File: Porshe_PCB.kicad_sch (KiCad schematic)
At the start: 37 parts, among them IC1 RASPBERRY_PI_PICO_W, J1 Conn_01x04_Socket, J10 Conn_01x03_Socket, J11 Conn_01x04_Socket, J12 Conn_01x01_Pin, J13 Conn_01x20_Socket, J2 SM04B-SRSS-TB_LF__SN_, J3 Conn_01x04_Socket, J4 S2B-PH-SM4-TB_LF__SN_, J5 Screw_Terminal_01x03, J6 Conn_01x01_Pin, J7 Conn_01x01_Pin, J8 Conn_01x01_Pin, J9 Conn_01x20_Socket, Q1 DMG2305UX-7, U1 DS3231SN, U2 AHT20

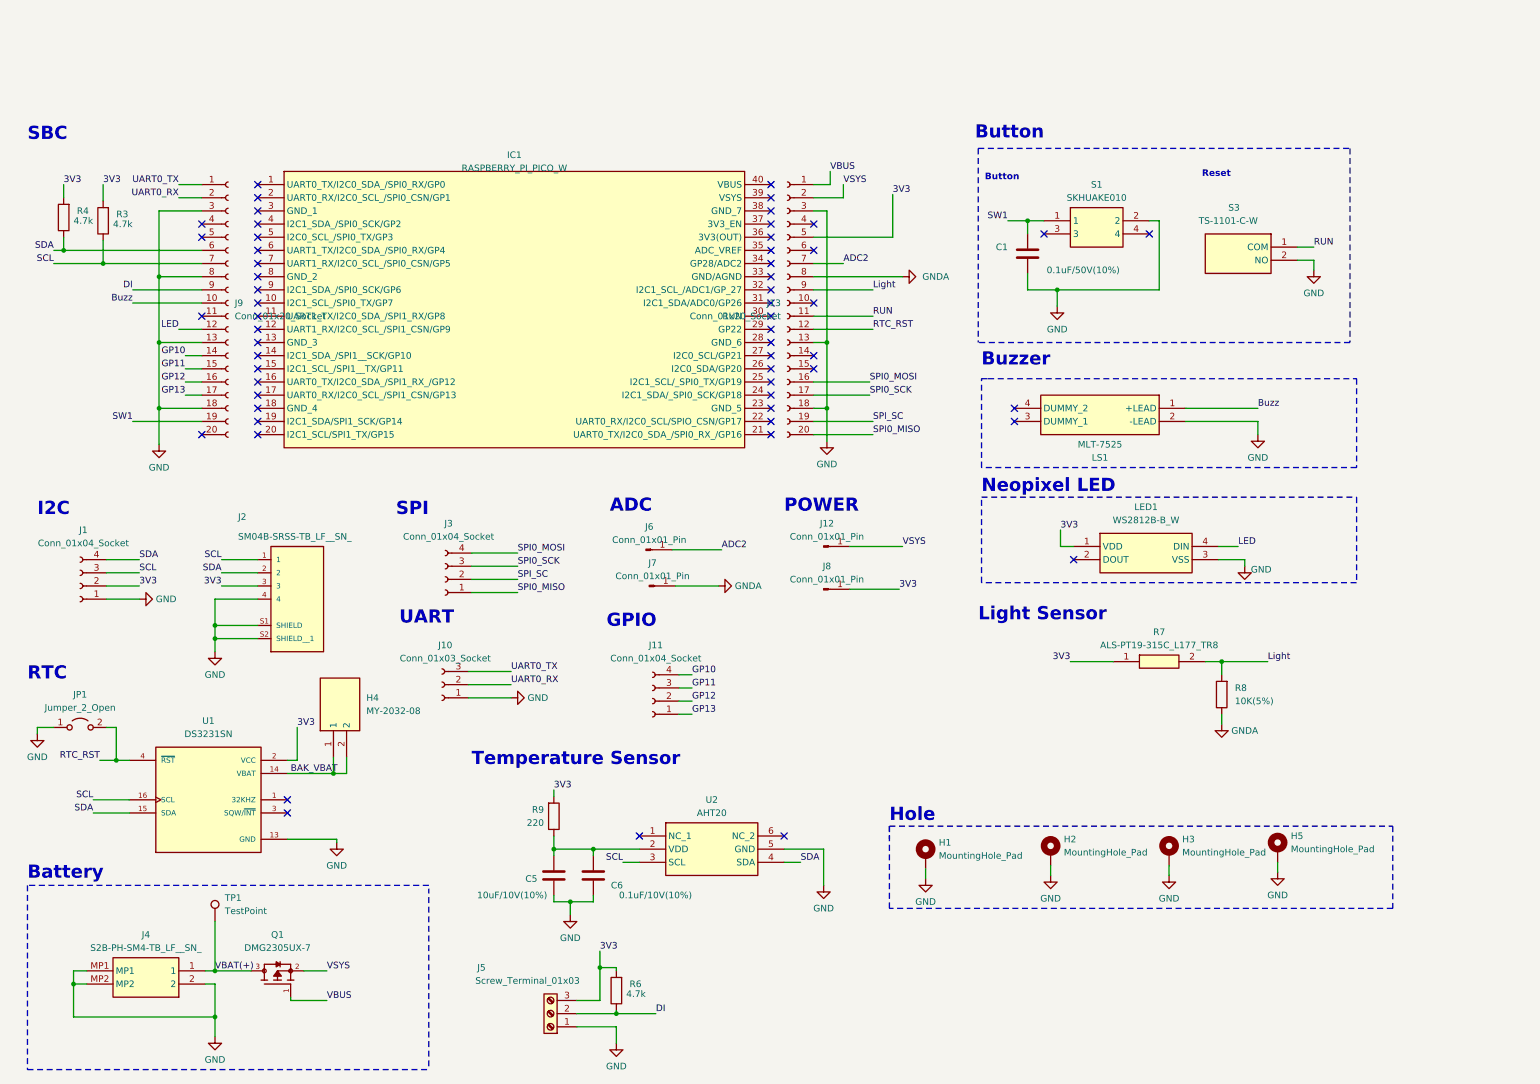
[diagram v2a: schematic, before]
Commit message: BOM확인후 부품 배치완료
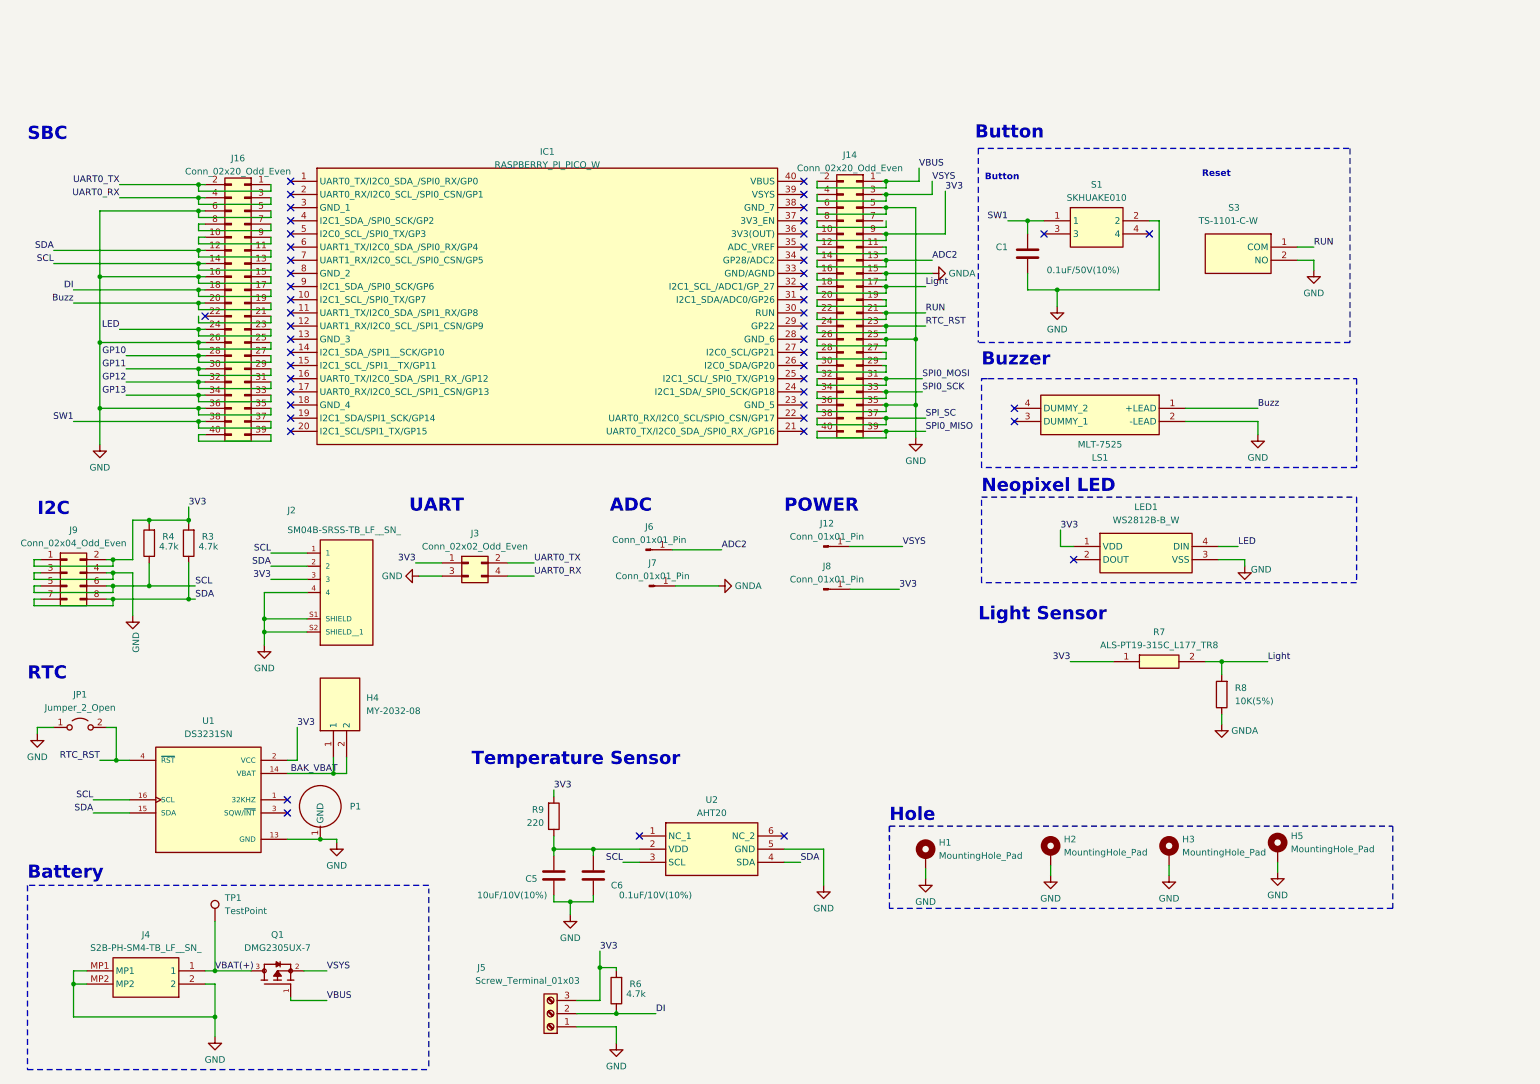
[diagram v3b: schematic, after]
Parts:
- removed J1, J11: Conn_01x04_Socket, symbol Connector:Conn_01x04_Socket
- removed J10: Conn_01x03_Socket, Connector_PinSocket_2.54mm:PinSocket_1x03_P2.54mm_Vertical_SMD_Pin1Left, symbol Connector:Conn_01x03_Socket
- removed J13: Conn_01x20_Socket, Connector_PinSocket_2.54mm:PinSocket_1x20_P2.54mm_Vertical_SMD_Pin1Right, symbol Connector:Conn_01x20_Socket
- removed J3: Conn_01x04_Socket, Connector_PinSocket_2.54mm:PinSocket_1x04_P2.54mm_Vertical, symbol Connector:Conn_01x04_Socket
- removed J9: Conn_01x20_Socket, Connector_PinSocket_2.54mm:PinSocket_1x20_P2.54mm_Vertical_SMD_Pin1Left, symbol Connector:Conn_01x20_Socket
- added J14, J16: Conn_02x20_Odd_Even, Connector_PinSocket_2.54mm:PinSocket_2x20_P2.54mm_Vertical_SMD, symbol Connector_Generic:Conn_02x20_Odd_Even
- added J3: Conn_02x02_Odd_Even, Connector_PinSocket_2.54mm:PinSocket_2x02_P2.54mm_Vertical_SMD, symbol Connector_Generic:Conn_02x02_Odd_Even
- added J9: Conn_02x04_Odd_Even, Connector_PinSocket_2.54mm:PinSocket_2x04_P2.54mm_Vertical_SMD, symbol Connector_Generic:Conn_02x04_Odd_Even
- added P1: ~, ConCell_GND:CR2032_GND, symbol CoinCell_GND:CR2032_GND
- C1: footprint Capacitor_Tantalum_SMD:CP_EIA-1608-08_AVX-J_Pad1.25x1.05mm_HandSolder -> Capacitor_SMD:C_0603_1608Metric; LCSC Part # (none) -> C14663
- C5: footprint Capacitor_Tantalum_SMD:CP_EIA-1608-10_AVX-L_Pad1.25x1.05mm_HandSolder -> Capacitor_SMD:C_0603_1608Metric; LCSC Part # (none) -> C19702
- C6: footprint Capacitor_Tantalum_SMD:CP_EIA-1608-10_AVX-L_Pad1.25x1.05mm_HandSolder -> Capacitor_SMD:C_0603_1608Metric; LCSC Part # (none) -> C519438
- H1, H2, H3, H5, J12, J6, J7, J8, JP1, TP1: now left out of the parts list
- H4: JLCPCB Part # (none) -> C964831
- J2: LCSC Part # (none) -> C160404
- J4: LCSC Part # (none) -> C295747
- J5: LCSC Part # (none) -> C695630
- LED1: JLCPCB Part # (none) -> C2761795
- Q1: LCSC Part # (none) -> C150470
- R7: LCSC Part # (none) -> C146233
- U2: LCSC Part # (none) -> C2757850
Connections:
- net 3V3: now also J14.10 (Pin_10), J14.9 (Pin_9), J3.1 (Pin_1), J9.1 (Pin_1), J9.2 (Pin_2)
- net ADC2: now also J14.13 (Pin_13), J14.14 (Pin_14)
- net Buzz: now also J16.19 (Pin_19), J16.20 (Pin_20)
- net DI: now also J16.17 (Pin_17), J16.18 (Pin_18)
- net GND: now also J14.25 (Pin_25), J14.26 (Pin_26), J14.35 (Pin_35), J14.36 (Pin_36), J14.5 (Pin_5), J14.6 (Pin_6), J16.15 (Pin_15), J16.16 (Pin_16), J16.25 (Pin_25), J16.26 (Pin_26), J16.35 (Pin_35), J16.36 (Pin_36), J16.5 (Pin_5), J16.6 (Pin_6), J3.3 (Pin_3), J9.3 (Pin_3), J9.4 (Pin_4), P1.1 (GND)
- net GNDA: now also J14.15 (Pin_15), J14.16 (Pin_16)
- net GP10: now also J16.27 (Pin_27), J16.28 (Pin_28)
- net GP11: now also J16.29 (Pin_29), J16.30 (Pin_30)
- net GP12: now also J16.31 (Pin_31), J16.32 (Pin_32)
- net GP13: now also J16.33 (Pin_33), J16.34 (Pin_34)
- net LED: now also J16.23 (Pin_23), J16.24 (Pin_24)
- net Light: now also J14.17 (Pin_17), J14.18 (Pin_18)
- net RTC_RST: now also J14.23 (Pin_23), J14.24 (Pin_24)
- net RUN: now also J14.21 (Pin_21), J14.22 (Pin_22)
- net SCL: now also R4.1, J16.13 (Pin_13), J16.14 (Pin_14), J9.5 (Pin_5), J9.6 (Pin_6); no longer R3.1
- net SDA: now also R3.1, J16.11 (Pin_11), J16.12 (Pin_12), J9.7 (Pin_7), J9.8 (Pin_8); no longer R4.1
- net SPI0_MISO: now also J14.39 (Pin_39), J14.40 (Pin_40)
- net SPI0_MOSI: now also J14.31 (Pin_31), J14.32 (Pin_32)
- net SPI0_SCK: now also J14.33 (Pin_33), J14.34 (Pin_34)
- net SPI_SC: now also J14.37 (Pin_37), J14.38 (Pin_38)
- net SW1: now also J16.37 (Pin_37), J16.38 (Pin_38)
- net UART0_RX: now also J16.3 (Pin_3), J16.4 (Pin_4), J3.4 (Pin_4)
- net UART0_TX: now also J16.1 (Pin_1), J16.2 (Pin_2), J3.2 (Pin_2)
- net VBUS: now also J14.1 (Pin_1), J14.2 (Pin_2)
- net VSYS: now also J14.3 (Pin_3), J14.4 (Pin_4)
- new net: J16.10 (Pin_10), J16.9 (Pin_9)
- new net: J16.39 (Pin_39), J16.40 (Pin_40)
- new net: J16.7 (Pin_7), J16.8 (Pin_8)
- new net: J14.11 (Pin_11), J14.12 (Pin_12)
- new net: J14.19 (Pin_19), J14.20 (Pin_20)
- new net: J14.27 (Pin_27), J14.28 (Pin_28)
- new net: J14.29 (Pin_29), J14.30 (Pin_30)
- no-connect marks 58 -> 50
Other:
- note removed: "GPIO"
- note removed: "SPI"
- moved on the sheet: IC1, J2, R3, R4

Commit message: 회로도 완성
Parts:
- removed C5: 10uF/10V(10%), Capacitor_SMD:C_0603_1608Metric, symbol Device:C
- removed C6: 0.1uF/10V(10%), Capacitor_SMD:C_0603_1608Metric, symbol Device:C
- removed H5: MountingHole_Pad, MountingHole:MountingHole_2.7mm_M2.5_ISO7380_Pad_TopOnly, symbol Mechanical:MountingHole_Pad
- removed J5: Screw_Terminal_01x03, TerminalBlock_4Ucon:TerminalBlock_4Ucon_1x03_P3.50mm_Horizontal, symbol Connector:Screw_Terminal_01x03
- removed R7: ALS-PT19-315C_L177_TR8, ALSPT19315CL177TR8, symbol ALS-PT19-315C_L177_TR8:ALS-PT19-315C_L177_TR8
- removed U2: AHT20, AHT20, symbol AHT20:AHT20
- added C2: 1uF/50V(10%), Capacitor_SMD:C_0603_1608Metric, symbol Device:C
- added IC2: BH1750FVI-TR, WSOF6, symbol BH1750FVI-TR:BH1750FVI-TR
- added J1: TF-115, TF115, symbol TF-115:TF-115
- added J10, J11, J5: Conn_01x01_Pin, TestPoint:TestPoint_THTPad_D2.0mm_Drill1.0mm, symbol Connector:Conn_01x01_Pin
- added JP2: Jumper_2_Open, Jumper:SolderJumper-2_P1.3mm_Open_RoundedPad1.0x1.5mm, symbol Jumper:Jumper_2_Open
- added JP3: Jumper_2_Bridged, Jumper:SolderJumper-2_P1.3mm_Bridged_RoundedPad1.0x1.5mm, symbol Jumper:Jumper_2_Bridged
- added R1, R2: 4.7k, Resistor_SMD:R_0603_1608Metric_Pad0.98x0.95mm_HandSolder, symbol Device:R
- added R5: 1k, Resistor_SMD:R_0603_1608Metric_Pad0.98x0.95mm_HandSolder, symbol Device:R
- added R7: 10k, Resistor_SMD:R_0603_1608Metric_Pad0.98x0.95mm_HandSolder, symbol Device:R
- added TP2, TP3: TestPoint, TestPoint:TestPoint_Pad_D1.0mm, symbol Connector:TestPoint
- R8: value 10K(5%) -> 10k/1%
- R9: value 220 -> 10k/1%
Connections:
- net GP11 is gone; now on net SPI0_MOSI: J16.29 (Pin_29), J16.30 (Pin_30)
- net GP13 is gone; now on net LED: J16.33 (Pin_33), J16.34 (Pin_34)
- net 3V3: now also IC2.1 (VCC), J1.4 (VDD), J5.1 (Pin_1), JP2.1 (A), R1.2, R2.2, R5.2; no longer R9.2
- net DI: now also J10.1 (Pin_1)
- net GND: now also C2.1, IC2.3 (GND), J1.6 (VSS), J1.MP1, J1.MP2, J1.MP3, J1.MP4, J11.1 (Pin_1), R7.1
- net GNDA: no longer R8.1
- net LED: no longer J16.23 (Pin_23), J16.24 (Pin_24)
- net SCL: now also IC2.6 (SCL)
- net SDA: now also IC2.4 (SDA)
- net SPI0_MISO: now also J16.21 (Pin_21), J16.22 (Pin_22), J1.7 (DAT0); no longer J14.39 (Pin_39), J14.40 (Pin_40)
- net SPI0_MOSI: now also J1.3 (CMD); no longer J14.31 (Pin_31), J14.32 (Pin_32)
- net SPI0_SCK: now also J1.5 (CLX); no longer J14.33 (Pin_33), J14.34 (Pin_34)
- net SPI_SC: now also J16.23 (Pin_23), J16.24 (Pin_24), J1.1 (DAT2), R2.1; no longer J14.37 (Pin_37), J14.38 (Pin_38)
- net VBAT(+): now also R8.2, R9.2
- net at R9.1: now also R8.1, JP3.1 (A)
- net at J14.7 (Pin_7): now also J14.8 (Pin_8)
- net GP10 renamed SPI1_SCK
- net GP12 renamed Light_RST
- net Light_RST: now also IC2.5 (DVI)
- net Light renamed BAT_DIV
- net BAT_DIV: now also JP3.2 (B); no longer R8.2
- new net: J1.2 (CD/DAT3), R1.1
- new net: J1.8 (DAT1), TP2.1
- new net: J1.CD1, TP3.1
- new net: C2.2, R5.1
- new net: IC2.2 (ADDR), JP2.2 (B), R7.2
- new net: J14.31 (Pin_31), J14.32 (Pin_32)
- new net: J14.33 (Pin_33), J14.34 (Pin_34)
- new net: J14.37 (Pin_37), J14.38 (Pin_38)
- new net: J14.39 (Pin_39), J14.40 (Pin_40)
- no-connect marks 50 -> 47
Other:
- note added: "SDcard"
- note removed: "Temperature Sensor"
- moved on the sheet: R6

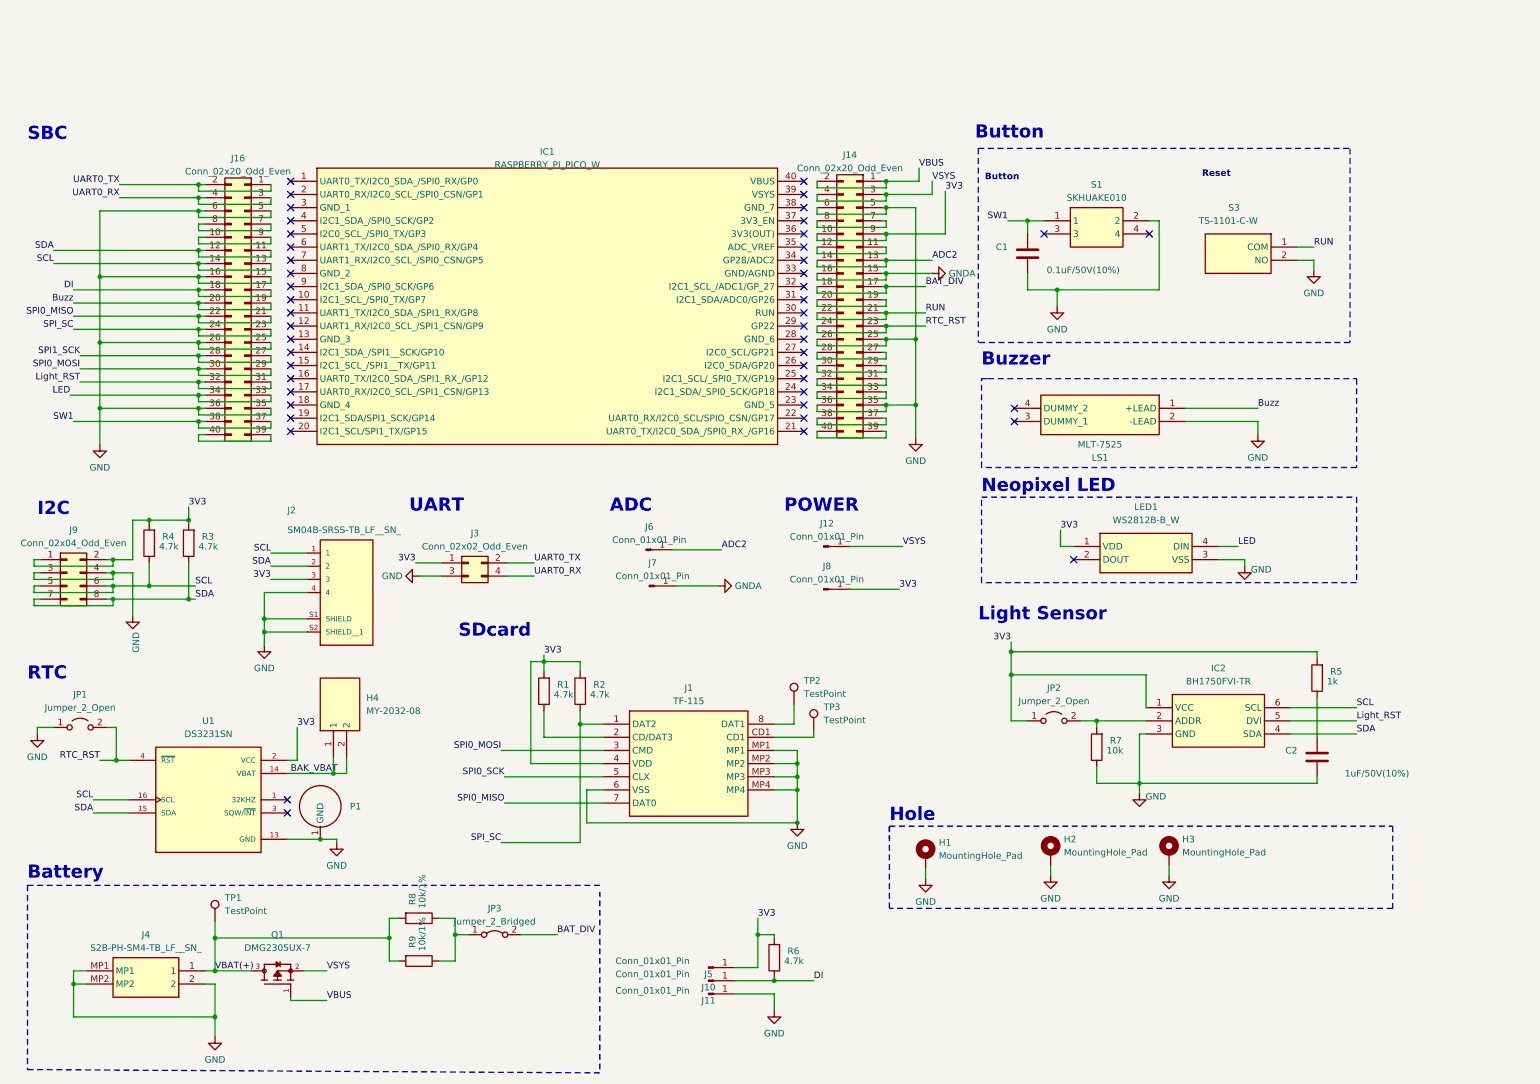
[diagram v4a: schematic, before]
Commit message: add smartfarm function
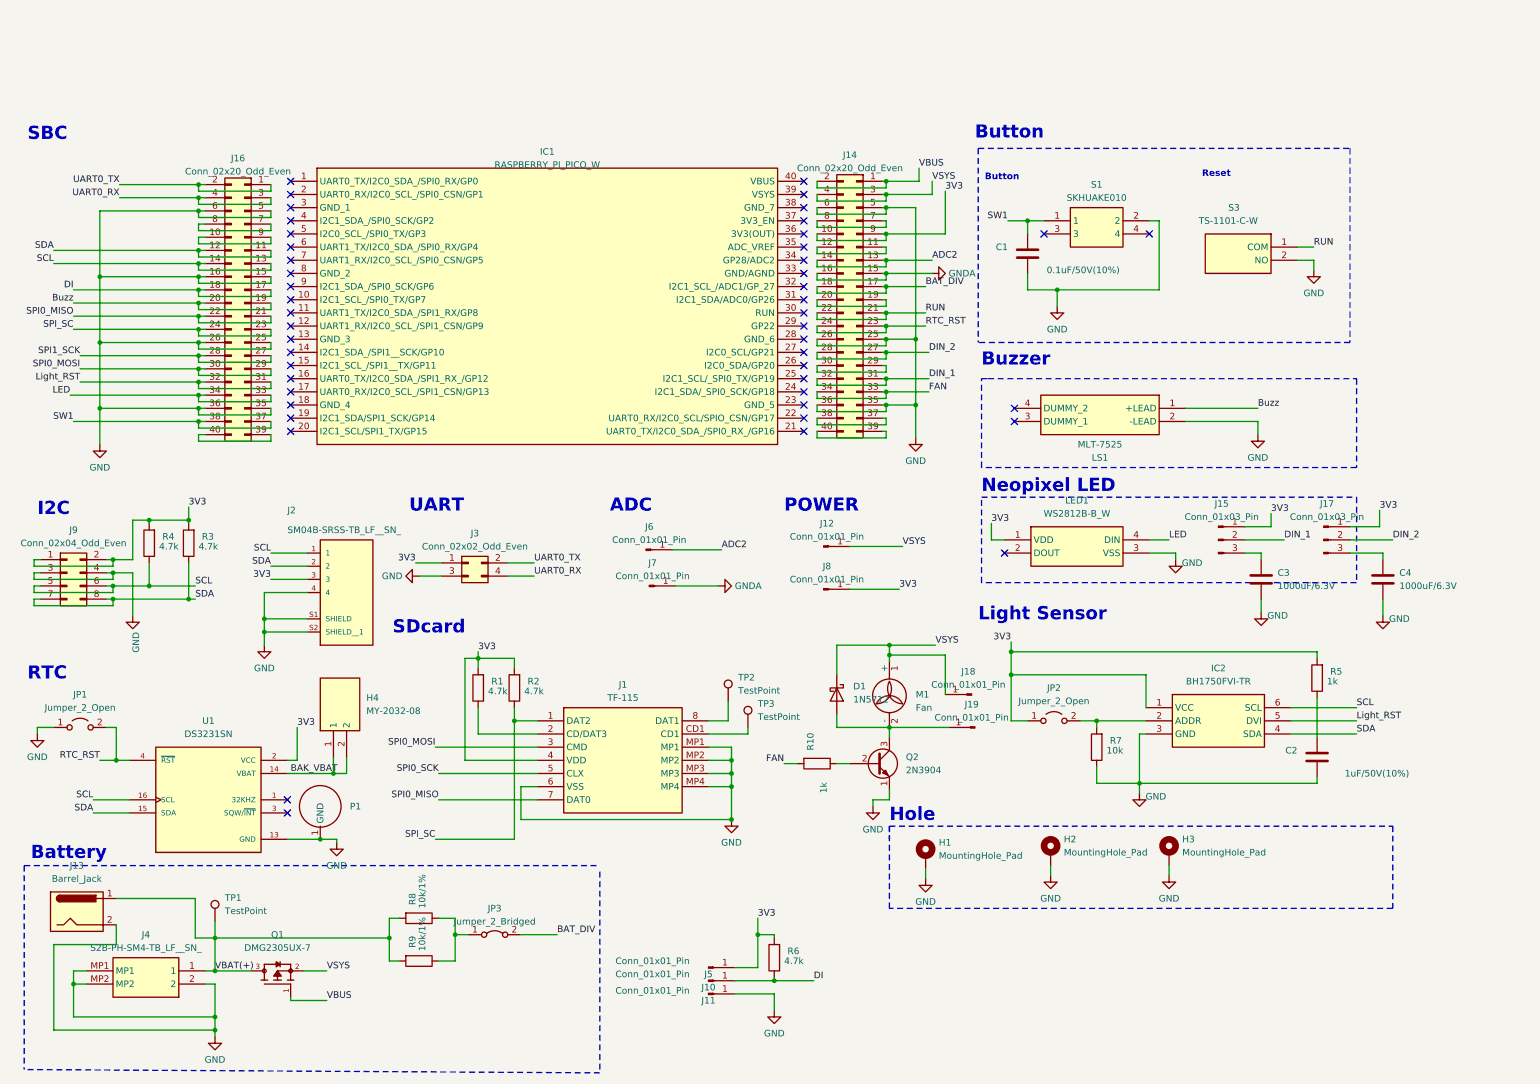
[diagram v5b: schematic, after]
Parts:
- added C3, C4: 1000uF/6.3V, Capacitor_THT:CP_Radial_D8.0mm_P5.00mm, symbol Device:C
- added D1: 1N5712, Diode_THT:D_DO-35_SOD27_P7.62mm_Horizontal, symbol Diode:1N5712
- added J13: Barrel_Jack, Connector_BarrelJack:BarrelJack_GCT_DCJ200-10-A_Horizontal, symbol Connector:Barrel_Jack
- added J15, J17: Conn_01x03_Pin, Connector_PinHeader_2.00mm:PinHeader_1x03_P2.00mm_Vertical, symbol Connector:Conn_01x03_Pin
- added J18, J19: Conn_01x01_Pin, Connector_Pin:Pin_D1.3mm_L11.0mm, symbol Connector:Conn_01x01_Pin
- added M1: Fan, symbol Motor:Fan
- added Q2: 2N3904, Package_TO_SOT_THT:TO-92_Inline, symbol Transistor_BJT:2N3904
- added R10: 1k, Resistor_SMD:R_0603_1608Metric_Pad0.98x0.95mm_HandSolder, symbol Device:R
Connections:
- net 3V3: now also J15.1 (Pin_1), J17.1 (Pin_1)
- net GND: now also C3.2, C4.2, J13.2, Q2.1 (E)
- net VBAT(+): now also J13.1
- net VSYS: now also D1.1 (K), J18.1 (Pin_1), M1.1 (+)
- net DIN_2: now reaches J14.27 (Pin_27), J14.28 (Pin_28)
- net DIN_2: now also J17.2 (Pin_2)
- net DIN_1: now reaches J14.31 (Pin_31), J14.32 (Pin_32)
- net DIN_1: now also J15.2 (Pin_2)
- net FAN: now reaches J14.33 (Pin_33), J14.34 (Pin_34)
- net FAN: now also R10.2
- new net: C3.1, J15.3 (Pin_3)
- new net: Q2.2 (B), R10.1
- new net: D1.2 (A), J19.1 (Pin_1), M1.2 (-), Q2.3 (C)
- new net: C4.1, J17.3 (Pin_3)
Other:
- moved on the sheet: J1, LED1, R1, R2, TP2, TP3
